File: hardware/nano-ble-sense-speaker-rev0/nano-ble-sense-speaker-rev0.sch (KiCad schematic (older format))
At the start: 8 parts, among them J1 Arduino-NANO-33, J2 Conn_01x02_Female, U1 LM78L05_TO92

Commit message: Added bar LED and a type C library
The plan is to later use a type C port to power the circuit.
Currently there is also a library that got updated in kicad but not in our project hence it will also need updating.

Signed-off-by: Dhruva Gole <goledhruva@gmail.com>
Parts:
- added BAR?: HDSP-4830_2, Display:HDSP-4830, symbol LED:HDSP-4830_2
- added D?: D_Schottky, symbol Device:D_Schottky
- U1: symbol Linear-reg:LM78L05_TO92 -> nano-ble-sense-speaker-rev0-rescue:LM78L05_TO92-Linear-reg
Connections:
- net +9V: now also D?.2 (A); no longer C1.1, U1.3 (VI)
- new net: C1.1, U1.3 (VI)
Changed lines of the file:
@@
 	3750 1250 3750 1300
 $Comp
-L Linear-reg:LM78L05_TO92 U1
+L nano-ble-sense-speaker-rev0-rescue:LM78L05_TO92-Linear-reg U1
 U 1 1 616D28C0
 P 3750 950
@@
 L power:+9V #PWR0103
 U 1 1 61703537
-P 3000 950
-F 0 "#PWR0103" H 3000 800 50  0001 C CNN
-F 1 "+9V" H 3015 1123 50  0000 C CNN
-F 2 "" H 3000 950 50  0001 C CNN
-F 3 "" H 3000 950 50  0001 C CNN
-	1    3000 950
-	1    0    0    -1
-$EndComp
-Wire Wire Line
-	3000 950  3200 950
-Connection ~ 3200 950
+P 2750 950
+F 0 "#PWR0103" H 2750 800 50  0001 C CNN
+F 1 "+9V" H 2765 1123 50  0000 C CNN
+F 2 "" H 2750 950 50  0001 C CNN
+F 3 "" H 2750 950 50  0001 C CNN
+	1    2750 950
+	1    0    0    -1
+$EndComp
 $Comp
 L Connector:Conn_01x02_Female J2
@@
 $EndComp
 Wire Wire Line
-	3000 950  3000 1750
-Wire Wire Line
-	3000 1750 3550 1750
-Connection ~ 3000 950
+	2750 950  2750 1750
 Wire Wire Line
 	3200 1300 3200 1850
@@
 	3950 2150 3950 2250
 Connection ~ 3950 2250
+$Comp
+L LED:HDSP-4830_2 BAR?
+U 1 1 61C9BEEE
+P 5800 1400
+F 0 "BAR?" H 5800 2067 50  0000 C CNN
+F 1 "HDSP-4830_2" H 5800 1976 50  0000 C CNN
+F 2 "Display:HDSP-4830" H 5800 600 50  0001 C CNN
+F 3 "https://docs.broadcom.com/docs/AV02-1798EN" H 3800 1600 50  0001 C CNN
+	1    5800 1400
+	1    0    0    -1
+$EndComp
+$Comp
+L Device:D_Schottky D?
+U 1 1 61CA4EDA
+P 3000 950
+F 0 "D?" H 3000 733 50  0000 C CNN
+F 1 "D_Schottky" H 3000 824 50  0000 C CNN
+F 2 "" H 3000 950 50  0001 C CNN
+F 3 "~" H 3000 950 50  0001 C CNN
+	1    3000 950
+	-1   0    0    1
+$EndComp
+Wire Wire Line
+	2850 950  2750 950
+Connection ~ 2750 950
+Wire Wire Line
+	2750 1750 3550 1750
 $EndSCHEMATC

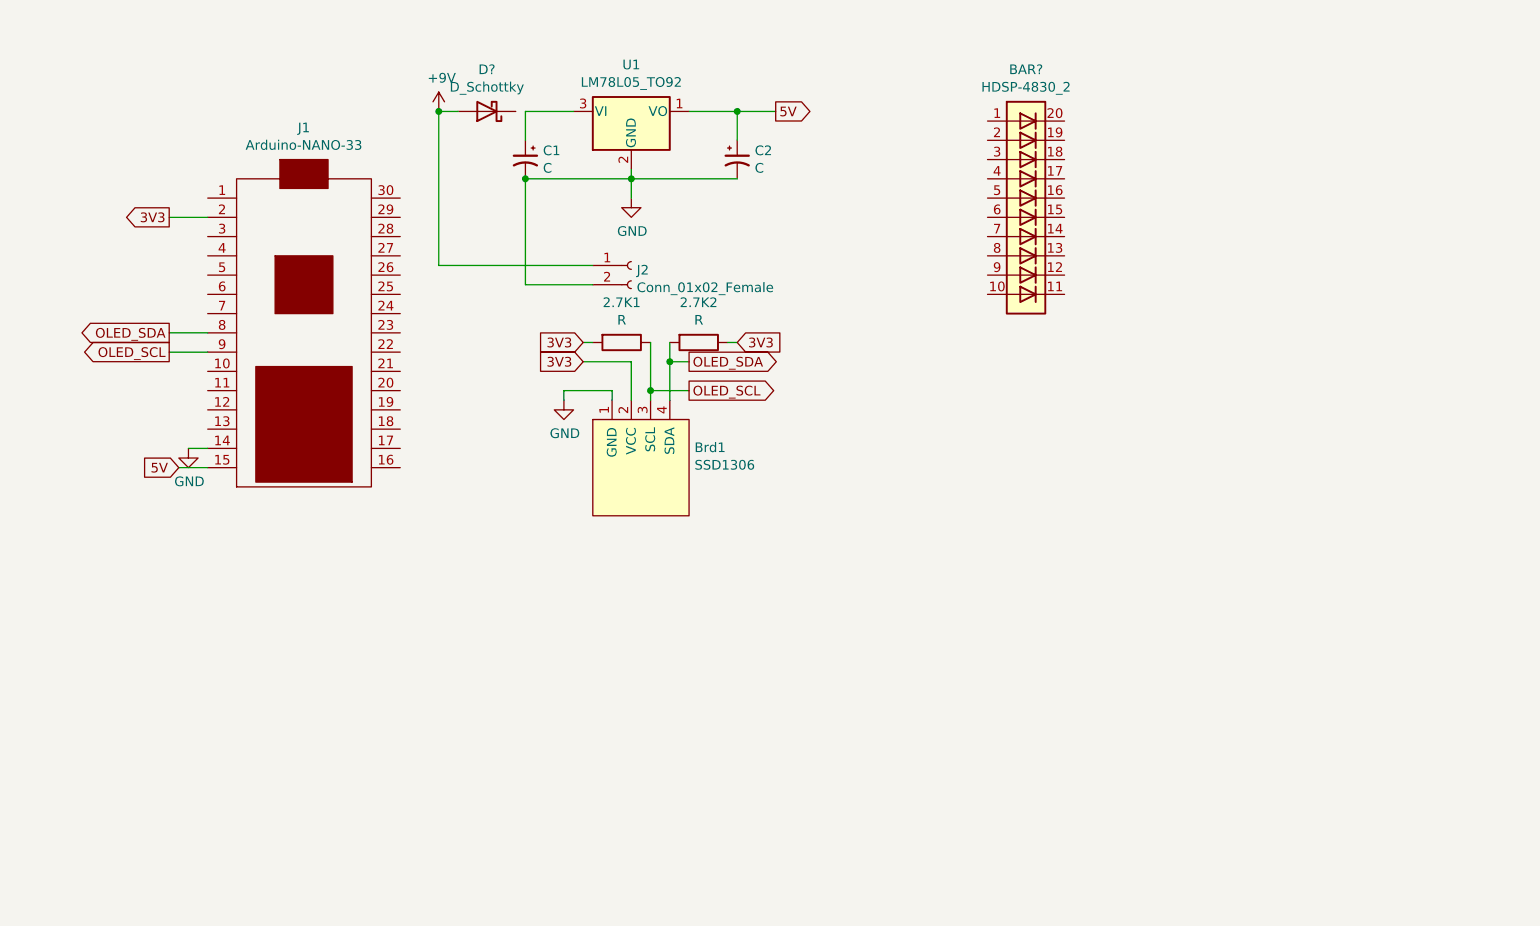
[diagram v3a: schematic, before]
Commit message: Update PCB design
- Now includes bar LED with all it's connections
- 3D files for OLED and arduino

TODO:
- Draw traces
- Make drill holes for mounting the OLED steadily
- Probably add a Li ion charging circuit

Signed-off-by: Dhruva Gole <goledhruva@gmail.com>
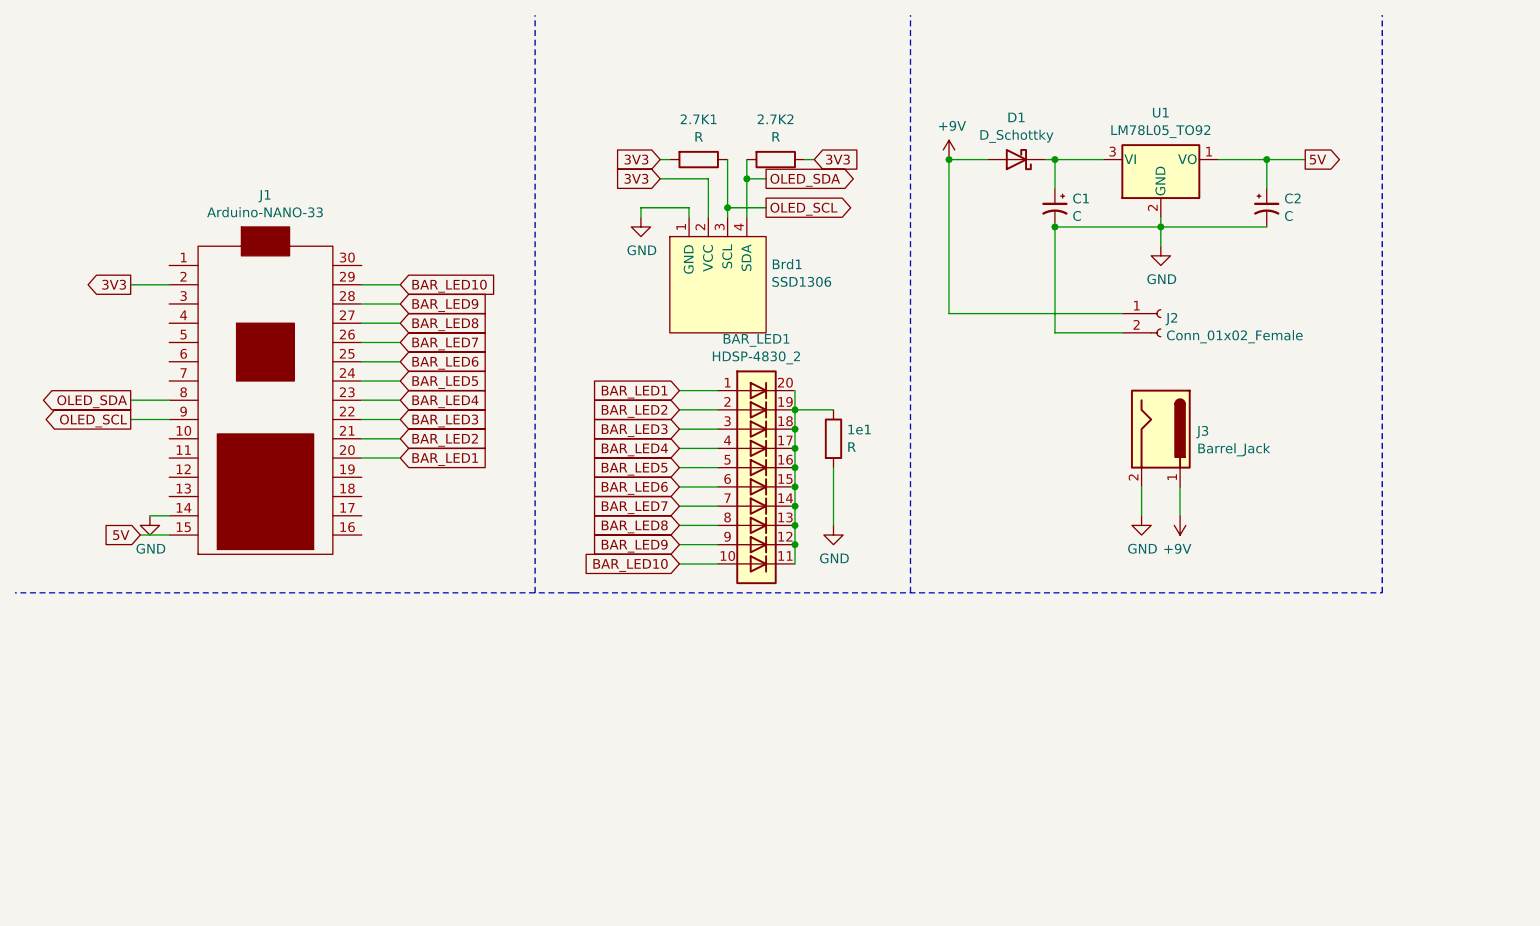
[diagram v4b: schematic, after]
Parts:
- added 1e1: R, Resistor_THT:R_Axial_DIN0207_L6.3mm_D2.5mm_P10.16mm_Horizontal, symbol Device:R
- added J3: Barrel_Jack, Connector_BarrelJack:BarrelJack_Horizontal, symbol Connector:Barrel_Jack
- 2.7K1, 2.7K2: footprint Resistor_SMD:R_0603_1608Metric_Pad0.98x0.95mm_HandSolder -> Resistor_THT:R_Axial_DIN0207_L6.3mm_D2.5mm_P10.16mm_Horizontal
- D1: renamed from D?; footprint (none) -> Diode_SMD:D_SOD-123
- gave numbers to parts that had none: 1
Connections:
- net +9V: now also J3.1
- net GND: now also 1e1.2, J3.2
- net BAR_LED1: now reaches J1.20
- net BAR_LED1: now also BAR_LED1.1 (A)
- net BAR_LED2: now reaches J1.21
- net BAR_LED2: now also BAR_LED1.2 (A)
- net BAR_LED3: now reaches J1.22
- net BAR_LED3: now also BAR_LED1.3 (A)
- net BAR_LED4: now reaches J1.23
- net BAR_LED4: now also BAR_LED1.4 (A)
- net BAR_LED5: now reaches J1.24
- net BAR_LED5: now also BAR_LED1.5 (A)
- net BAR_LED6: now reaches J1.25
- net BAR_LED6: now also BAR_LED1.6 (A)
- net BAR_LED7: now reaches J1.26
- net BAR_LED7: now also BAR_LED1.7 (A)
- net BAR_LED8: now reaches J1.27
- net BAR_LED8: now also BAR_LED1.8 (A)
- net BAR_LED9: now reaches J1.28
- net BAR_LED9: now also BAR_LED1.9 (A)
- net BAR_LED10: now reaches J1.29
- net BAR_LED10: now also BAR_LED1.10 (A)
- net at C1.1, U1.3 (VI): now also D1.1 (K)
- net at BAR_LED1.11 (K): now also BAR_LED1.12 (K), BAR_LED1.13 (K), BAR_LED1.14 (K), BAR_LED1.15 (K), BAR_LED1.16 (K), BAR_LED1.17 (K), BAR_LED1.18 (K), BAR_LED1.19 (K), BAR_LED1.20 (K), 1e1.1
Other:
- moved on the sheet: 2.7K1, 2.7K2, BAR_LED1, Brd1, C1, C2, D1, J1, J2, U1

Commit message: Minor changes
Signed-off-by: Dhruva Gole <goledhruva@gmail.com>
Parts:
- added MQ_Conn1: Conn_01x04_Male, MQ-sensor:MQ-3, symbol Connector:Conn_01x04_Male
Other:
- note added: "MQ sensor"
- note added: "Microcontroller"
- note added: "Power Section"
- note added: "UI Components"
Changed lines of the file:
@@
 Wire Notes Line width 20 style dash_dot rgb(194, 1, 0)
 	7650 3450 7650 450
+$Comp
+L Connector:Conn_01x04_Male MQ_Conn1
+U 1 1 61CBB754
+P 7900 1300
+F 0 "MQ_Conn1" H 8008 1581 50  0000 C CNN
+F 1 "Conn_01x04_Male" H 8008 1490 50  0000 C CNN
+F 2 "MQ-sensor:MQ-3" H 7900 1300 50  0001 C CNN
+F 3 "~" H 7900 1300 50  0001 C CNN
+	1    7900 1300
+	1    0    0    -1
+$EndComp
+Text Notes 1550 850  0    50   ~ 0
+Microcontroller
+Text Notes 4050 700  0    50   ~ 0
+UI Components
+Text Notes 6200 700  0    50   ~ 0
+Power Section
+Text Notes 7750 600  0    50   ~ 0
+MQ sensor
 $EndSCHEMATC
